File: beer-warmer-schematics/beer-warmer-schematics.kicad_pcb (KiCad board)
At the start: 4 copper layers, 60 x 42.8 mm, 41 parts, among them J1 USB_C_Receptacle_USB2.0_14P, J2 Screw_Terminal_01x02, J3 Conn_01x07_Socket, J4 Conn_01x07_Socket, J5 Conn_01x04_Pin, J6 Screw_Terminal_01x03, Q1 AOD4184A, U2 LM2596S-5, U3 CH224K, U4 INA219AxDCN

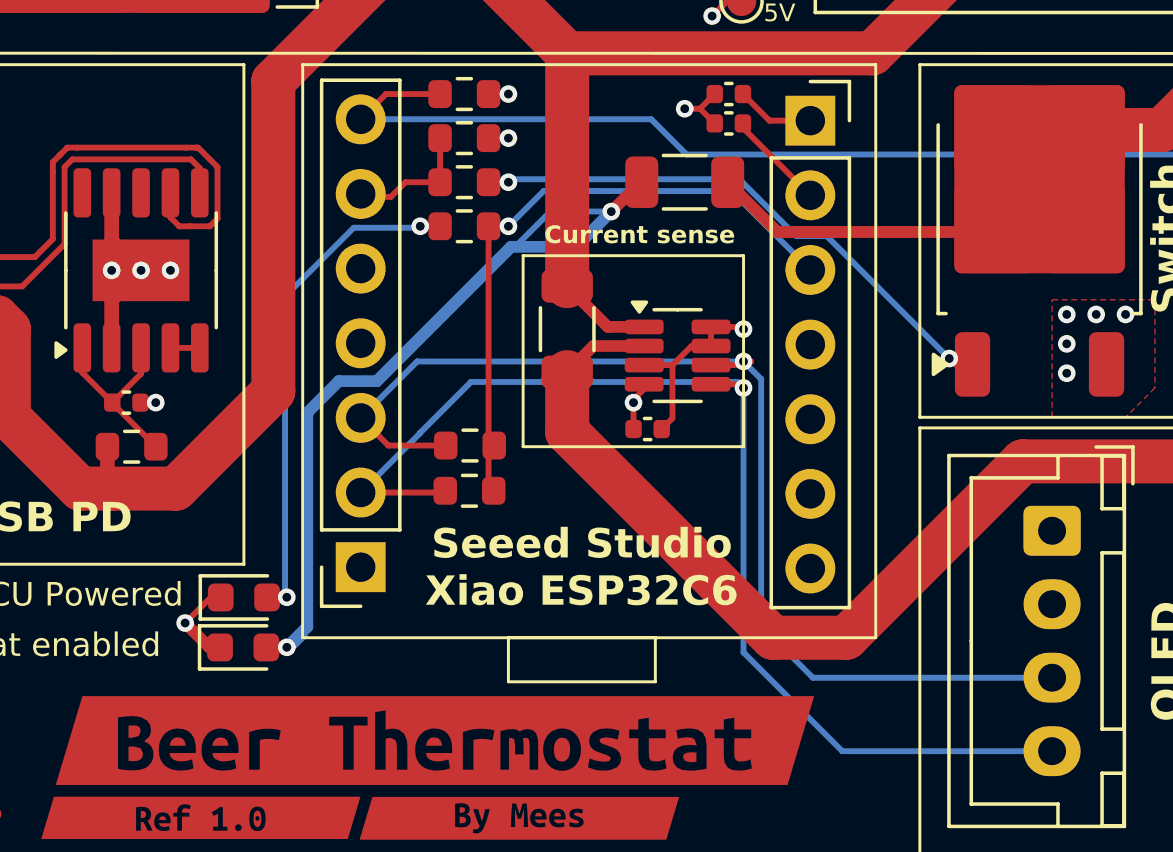
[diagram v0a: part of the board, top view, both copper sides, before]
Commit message: fix active led, bottom silkscreen
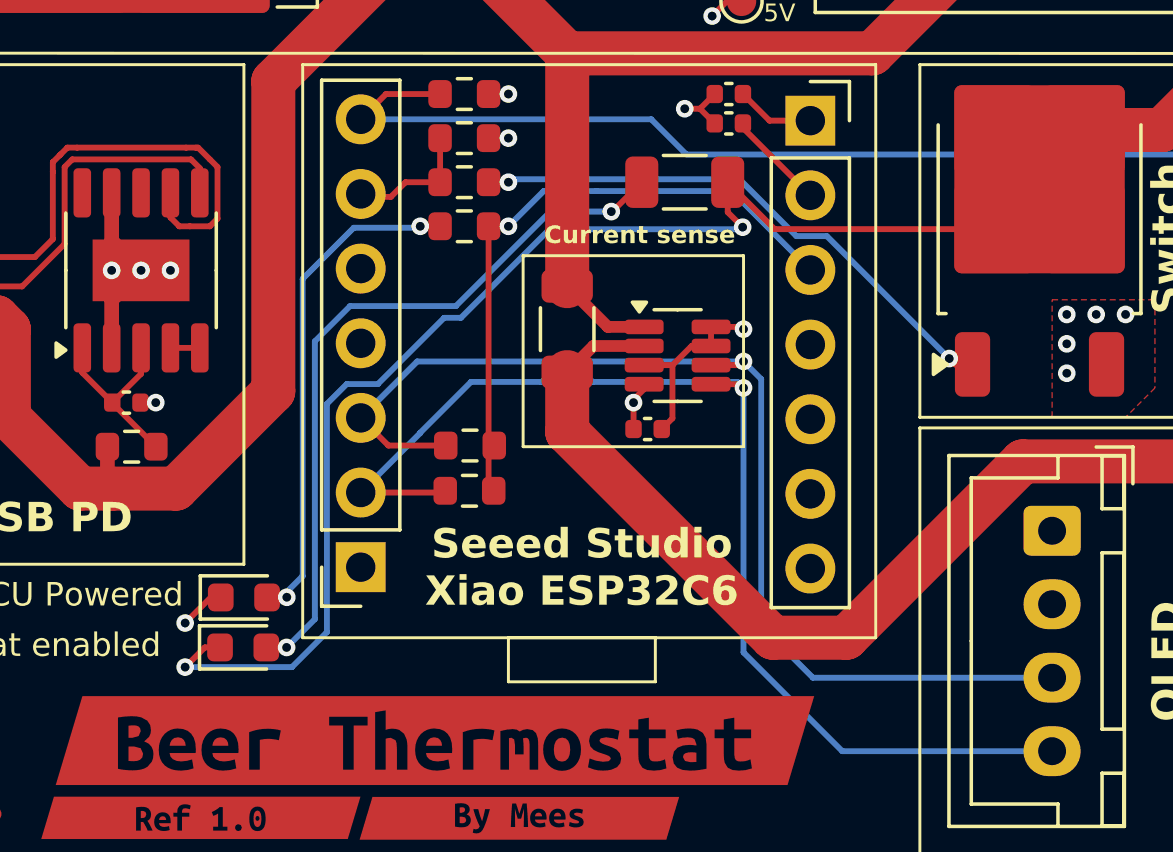
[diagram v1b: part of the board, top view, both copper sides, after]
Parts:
- J1: value USB_C_Receptacle_USB2.0_14P -> USB_C_Receptacle_6P
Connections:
- D2 pad 1: GND -> HEAT-
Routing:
- net HEAT-: track 32.5 -> 55.8 mm, vias 0 -> 2
- net Net-(D2-A): track 45.4 -> 24.5 mm
- net GND: track 42.8 -> 41.3 mm
- net SDA: track 38.7 -> 38.1 mm
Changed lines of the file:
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@@
 			(layers "F.Cu" "F.Mask" "F.Paste")
 			(roundrect_rratio 0.25)
-			(net 22 "GND")
+			(net 24 "HEAT-")
 			(pinfunction "K")
 			(pintype "passive")
@@
 			)
 		)
-		(property "Value" "USB_C_Receptacle_USB2.0_14P"
+		(property "Value" "USB_C_Receptacle_6P"
 			(at 0 4.725 270)
 			(unlocked yes)
@@
 		(layer "F.SilkS")
 	)
+	(gr_rect
+		(start 169.5 79.5)
+		(end 179 89.5)
+		(stroke
+			(width 0.1)
+			(type default)
+		)
+		(fill no)
+		(layer "B.SilkS")
+	)
+	(gr_rect
+		(start 169.5 91)
+		(end 179 106)
+		(stroke
+			(width 0.1)
+			(type default)
+		)
+		(fill no)
+		(layer "B.SilkS")
+	)
 	(gr_line
 		(start 182 110)
@@
 		)
 	)
+	(gr_text "-\n\n\n+"
+		(at 172.5 87.5 0)
+		(layer "B.SilkS")
+		(effects
+			(font
+				(size 1 1)
+				(thickness 0.2)
+				(bold yes)
+			)
+			(justify left bottom mirror)
+		)
+	)
 	(gr_text "Heater\nout"
-		(at 171.5 86.58 0)
+		(at 169 82.5 0)
 		(layer "B.SilkS")
 		(effects
@@
 		)
 	)
-	(gr_text "SIG\n5V\nGND"
-		(at 171.5 101.58 0)
+	(gr_text "SIG\n\n\n5V\n\n\nGND"
+		(at 173 104 0)
 		(layer "B.SilkS")
 		(effects
 			(font
-				(size 1.5 1.5)
-				(thickness 0.3)
+				(size 1 1)
+				(thickness 0.2)
 				(bold yes)
 			)
@@
 	)
 	(gr_text "Temp\nprobe"
-		(at 171.5 94.08 0)
+		(at 168.778727 93.941909 0)
 		(layer "B.SilkS")
 		(effects
@@
 	)
 	(segment
-		(start 149.5375 91)
-		(end 149.5 91)
-		(width 0.4)
+		(start 148.5 92)
+		(end 148.5375 92)
+		(width 0.2)
 		(layer "F.Cu")
 		(net 4)
 	)
 	(segment
-		(start 137.456833 106.829694)
-		(end 137.460788 106.825739)
-		(width 0.4)
+		(start 136.762359 106.830388)
+		(end 136.761665 106.829694)
+		(width 0.2)
 		(layer "F.Cu")
 		(net 4)
 	)
 	(segment
-		(start 149.5 91)
-		(end 148.5 92)
+		(start 149.5375 91)
+		(end 149.5 91)
 		(width 0.4)
 		(layer "F.Cu")
@@
 	)
 	(segment
-		(start 136.761665 106.829694)
-		(end 137.456833 106.829694)
-		(width 0.4)
+		(start 148.5375 92)
+		(end 149.5375 91)
+		(width 0.2)
 		(layer "F.Cu")
 		(net 4)
@@
 	)
 	(via
-		(at 137.460788 106.825739)
+		(at 137.452508 106.830388)
 		(size 0.6)
 		(drill 0.3)
@@
 	)
 	(segment
-		(start 148.5 92)
-		(end 147.299 93.201)
-		(width 0.4)
-		(layer "B.Cu")
-		(net 4)
-	)
-	(segment
-		(start 138.160531 98.839469)
-		(end 138.160531 106.125996)
-		(width 0.4)
-		(layer "B.Cu")
-		(net 4)
-	)
-	(segment
-		(start 138.160531 106.125996)
-		(end 137.460788 106.825739)
-		(width 0.4)
-		(layer "B.Cu")
-		(net 4)
-	)
-	(segment
-		(start 138.060531 98.939469)
-		(end 138.060531 106.221217)
-		(width 0.2)
-		(layer "B.Cu")
-		(net 4)
-	)
-	(segment
-		(start 146.4279 92)
-		(end 140.5589 97.869)
+		(start 138.41362 105.869276)
+		(end 137.452508 106.830388)
 		(width 0.2)
 		(layer "B.Cu")
@@
 	)
 	(segment
-		(start 139.231 97.769)
-		(end 138.160531 98.839469)
-		(width 0.4)
-		(layer "B.Cu")
-		(net 4)
-	)
-	(segment
-		(start 147.299 93.201)
-		(end 145.08548 93.201)
-		(width 0.4)
-		(layer "B.Cu")
-		(net 4)
-	)
-	(segment
 		(start 148.5 92)
 		(end 146.4279 92)
@@
 	)
 	(segment
-		(start 138.060531 106.221217)
-		(end 138.060531 106.439469)
+		(start 138.41362 96.41362)
+		(end 138.41362 105.869276)
 		(width 0.2)
 		(layer "B.Cu")
@@
 	)
 	(segment
-		(start 145.08548 93.201)
-		(end 140.51748 97.769)
-		(width 0.4)
-		(layer "B.Cu")
-		(net 4)
-	)
-	(segment
-		(start 138.060531 106.439469)
-		(end 137.5 107)
+		(start 139.61329 95.21395)
+		(end 138.41362 96.41362)
 		(width 0.2)
 		(layer "B.Cu")
@@
 	)
 	(segment
-		(start 140.5589 97.869)
-		(end 139.131 97.869)
+		(start 143.21395 95.21395)
+		(end 139.61329 95.21395)
 		(width 0.2)
 		(layer "B.Cu")
@@
 	)
 	(segment
-		(start 140.51748 97.769)
-		(end 139.231 97.769)
-		(width 0.4)
-		(layer "B.Cu")
-		(net 4)
-	)
-	(segment
-		(start 139.131 97.869)
-		(end 138.060531 98.939469)
+		(start 146.4279 92)
+		(end 143.21395 95.21395)
 		(width 0.2)
 		(layer "B.Cu")
@@
 	)
 	(segment
-		(start 153.25747 97.099)
-		(end 153.132467 97.224003)
+		(start 151.89497 97.224003)
+		(end 152.874997 97.224003)
 		(width 0.2)
 		(layer "F.Cu")
@@
 	)
 	(segment
-		(start 153.132467 97.224003)
-		(end 151.89497 97.224003)
+		(start 152.874997 97.224003)
+		(end 153 97.099)
 		(width 0.2)
 		(layer "F.Cu")
@@
 	)
 	(segment
-		(start 153.25747 97.099)
-		(end 141.896 97.099)
+		(start 155.360525 107.860525)
+		(end 153.601 106.101)
 		(width 0.2)
 		(layer "B.Cu")
@@
 	)
 	(segment
-		(start 155.360525 107.860525)
-		(end 153.601 106.101)
+		(start 141.896 97.099)
+		(end 139.975 99.02)
 		(width 0.2)
 		(layer "B.Cu")
@@
 	)
 	(segment
-		(start 141.896 97.099)
-		(end 139.975 99.02)
+		(start 153 97.099)
+		(end 141.896 97.099)
 		(width 0.2)
 		(layer "B.Cu")
@@
 	)
 	(segment
-		(start 142 92.5)
-		(end 141.949 92.551)
+		(start 141.949 92.551)
+		(end 139.73624 92.551)
 		(width 0.2)
 		(layer "B.Cu")
@@
 	)
 	(segment
-		(start 141.949 92.551)
-		(end 139.73624 92.551)
+		(start 138 94.28724)
+		(end 138 104.4)
+		(width 0.2)
+		(layer "B.Cu")
+		(net 20)
+	)
+	(segment
+		(start 138 104.4)
+		(end 137.4 105)
 		(width 0.2)
 		(layer "B.Cu")
@@
 	(segment
 		(start 139.73624 92.551)
-		(end 137.4 94.88724)
+		(end 138 94.28724)
 		(width 0.2)
 		(layer "B.Cu")
@@
 	)
 	(segment
-		(start 137.4 94.88724)
-		(end 137.4 105)
+		(start 142 92.5)
+		(end 141.949 92.551)
 		(width 0.2)
 		(layer "B.Cu")
@@
 	)
 	(segment
-		(start 135.186665 106.829694)
-		(end 134.829694 106.829694)
-		(width 0.4)
-		(layer "F.Cu")
-		(net 22)
-	)
-	(segment
 		(start 131.5 91.3625)
 		(end 131.5 91.5)
@@
 	)
 	(segment
-		(start 134.829694 106.829694)
-		(end 134 106)
-		(width 0.4)
-		(layer "F.Cu")
-		(net 22)
-	)
-	(segment
 		(start 151.89497 95.924003)
 		(end 152.924003 95.924003)
@@
 	)
 	(segment
+		(start 134.670306 106.829694)
+		(end 134 107.5)
+		(width 0.2)
+		(layer "F.Cu")
+		(net 24)
+	)
+	(segment
 		(start 161.5475 92.575)
 		(end 161.426162 92.696338)
@@
 	)
 	(segment
-		(start 161.426162 92.696338)
-		(end 154.158838 92.696338)
-		(width 0.4)
+		(start 152.4625 91)
+		(end 152.4625 92.022128)
+		(width 0.2)
+		(layer "F.Cu")
+		(net 24)
+	)
+	(segment
+		(start 152.4625 92.022128)
+		(end 152.970186 92.529814)
+		(width 0.2)
 		(layer "F.Cu")
 		(net 24)
@@
 	)
 	(segment
-		(start 154.158838 92.696338)
-		(end 152.4625 91)
-		(width 0.4)
+		(start 135.186665 106.829694)
+		(end 134.670306 106.829694)
+		(width 0.2)
 		(layer "F.Cu")
 		(net 24)
 	)
+	(via
+		(at 152.970186 92.529814)
+		(size 0.6)
+		(drill 0.3)
+		(layers "F.Cu" "B.Cu")
+		(net 24)
+	)
+	(via
+		(at 134 107.5)
+		(size 0.6)
+		(drill 0.3)
+		(layers "F.Cu" "B.Cu")
+		(net 24)
+	)
+	(segment
+		(start 138.824 98.54324)
+		(end 138.824 106.308839)
+		(width 0.2)
+		(layer "B.Cu")
+		(net 24)
+	)
+	(segment
+		(start 152.970186 92.529814)
+		(end 152.899 92.601)
+		(width 0.2)
+		(layer "B.Cu")
+		(net 24)
+	)
+	(segment
+		(start 138.824 106.308839)
+		(end 137.632839 107.5)
+		(width 0.2)
+		(layer "B.Cu")
+		(net 24)
+	)
+	(segment
+		(start 152.899 92.601)
+		(end 146.399 92.601)
+		(width 0.2)
+		(layer "B.Cu")
+		(net 24)
+	)
+	(segment
+		(start 146.399 92.601)
+		(end 143.38505 95.61495)
+		(width 0.2)
+		(layer "B.Cu")
+		(net 24)
+	)
+	(segment
+		(start 137.632839 107.5)
+		(end 134 107.5)
+		(width 0.2)
+		(layer "B.Cu")
+		(net 24)
+	)
+	(segment
+		(start 139.49824 97.869)
+		(end 138.824 98.54324)
+		(width 0.2)
+		(layer "B.Cu")
+		(net 24)
+	)
+	(segment
+		(start 140.5589 97.869)
+		(end 139.49824 97.869)
+		(width 0.2)
+		(layer "B.Cu")
+		(net 24)
+	)
+	(segment
+		(start 142.81295 95.61495)
+		(end 140.5589 97.869)
+		(width 0.2)
+		(layer "B.Cu")
+		(net 24)
+	)
+	(segment
+		(start 143.38505 95.61495)
+		(end 142.81295 95.61495)
+		(width 0.2)
+		(layer "B.Cu")
+		(net 24)
+	)

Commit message: incorporated some feedback
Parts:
- removed C4: 1uF, Capacitor_SMD:C_0402_1005Metric
- moved R8 1.54 mm to (143.7, 101.5)
- moved R9 1.54 mm to (143.7, 100.0)
- moved C1 1.00 mm to (152.5, 89.0)
- turned R2 to 0 degrees
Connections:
- J3 pad 2: Net-(J3-Pin_2) -> GND
- R2 pad 1: GND -> D1
- R2 pad 2: D1 -> GND
- R8 pad 1: SDA -> SCL
- R9 pad 1: SCL -> SDA
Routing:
- net Net-(J3-Pin_2): track 3.40 -> 0.00 mm
- net GND: track 41.3 -> 39.9 mm

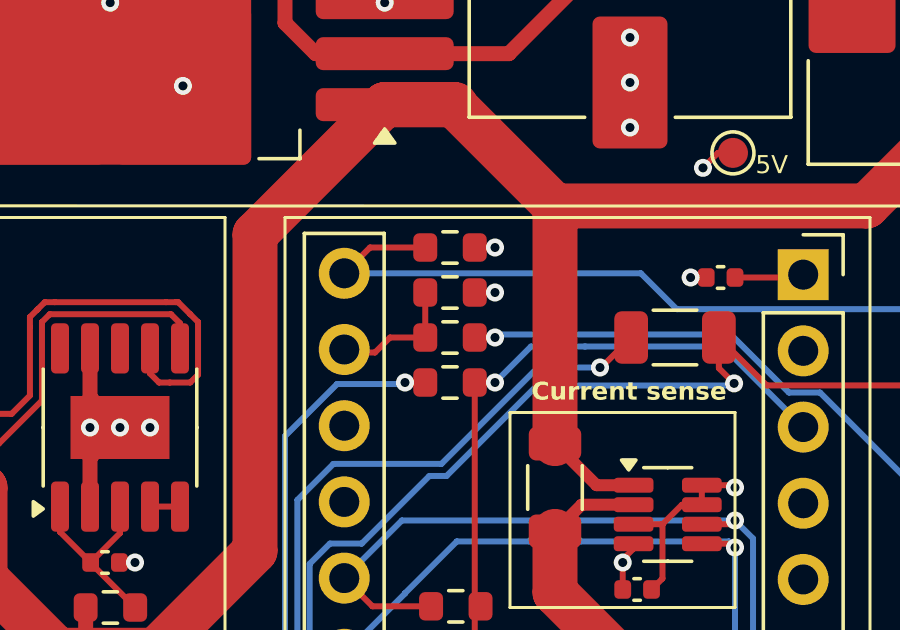
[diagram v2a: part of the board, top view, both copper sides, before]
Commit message: low side driver
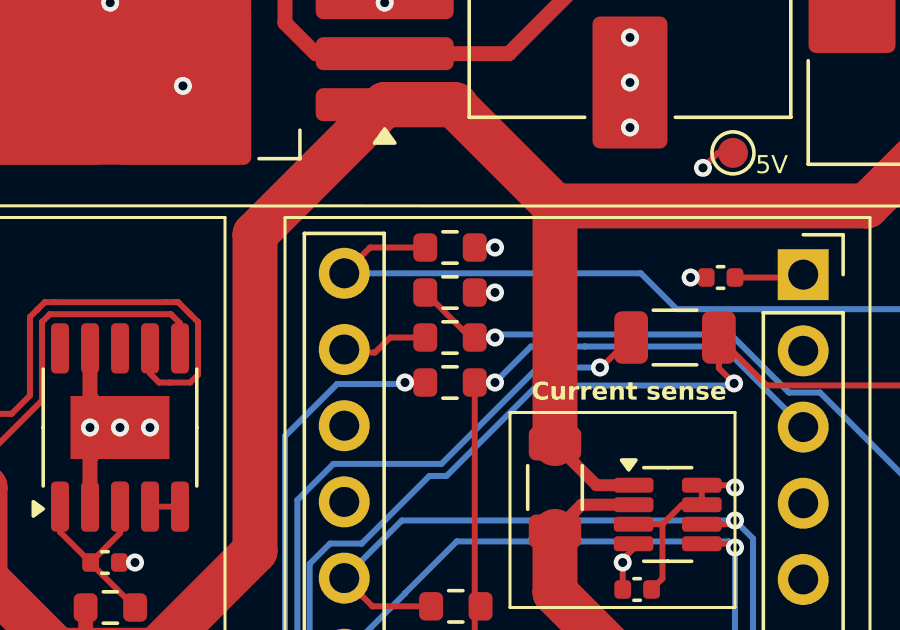
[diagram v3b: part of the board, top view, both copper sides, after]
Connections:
- R2 pad 1: D1 -> Net-(Q1-G)
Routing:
- net Net-(Q1-G): track 19.2 -> 21.5 mm
- net D1: track 5.01 -> 3.51 mm
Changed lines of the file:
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@@
 			(layers "F.Cu" "F.Mask" "F.Paste")
 			(roundrect_rratio 0.25)
-			(net 17 "D1")
+			(net 24 "Net-(Q1-G)")
 			(pintype "passive")
 		)
@@
 	)
 	(segment
-		(start 142.675 89.5)
-		(end 142.675 91)
-		(width 0.2)
-		(layer "F.Cu")
-		(net 17)
-	)
-	(segment
 		(start 140.835 88)
 		(end 142.675 88)
@@
 	)
 	(segment
+		(start 144.175 91)
+		(end 142.675 89.5)
+		(width 0.2)
+		(layer "F.Cu")
+		(net 24)
+	)
+	(segment
 		(start 144.325 91)
 		(end 144.902 91)
 		(width 0.2)
 		(layer "F.Cu")
+		(net 24)
+	)
+	(segment
+		(start 144.325 91)
+		(end 144.175 91)
+		(width 0.2)
+		(layer "F.Cu")

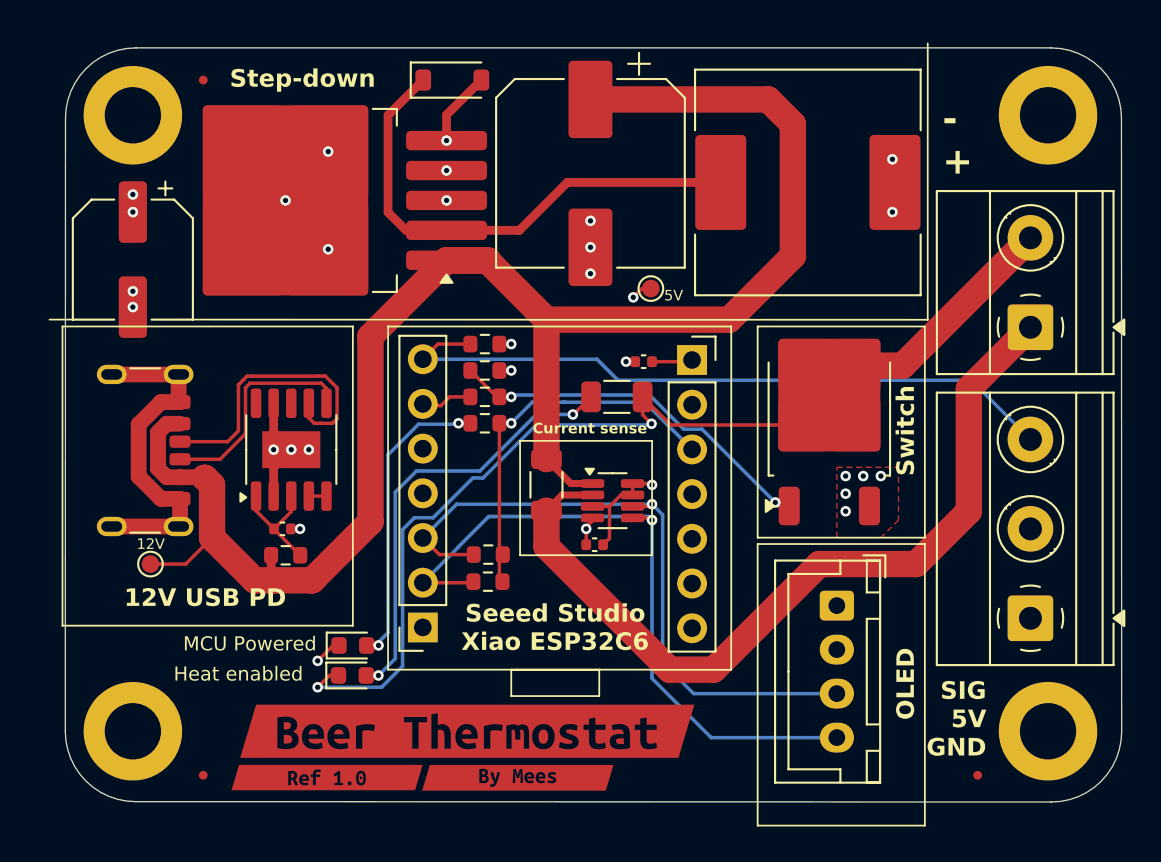
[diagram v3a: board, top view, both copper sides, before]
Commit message: different step down
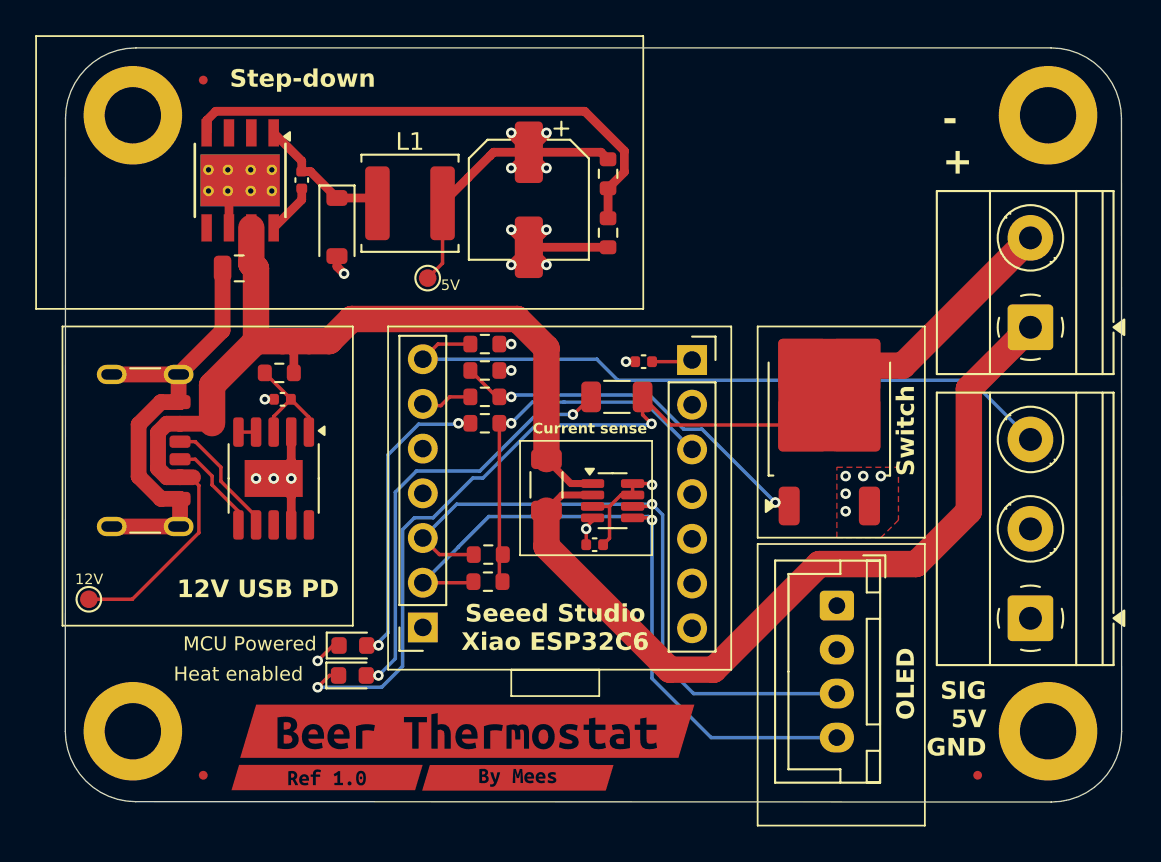
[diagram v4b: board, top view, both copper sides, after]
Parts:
- added C7: 10nF, Capacitor_SMD:C_0402_1005Metric, F.Cu at (133.1, 78.7)
- added R11: 3.3K, Resistor_SMD:R_0603_1608Metric, F.Cu at (150.5, 81.7)
- added R5: 10K, Resistor_SMD:R_0603_1608Metric, F.Cu at (150.5, 78.3)
- C2: value 680uF -> 10uF; footprint Capacitor_SMD:CP_Elec_10x10.5 -> Capacitor_SMD:C_0805_2012Metric
- L1: value 33uH -> 15uH; footprint Inductor_SMD:L_SXN_SMDRI127 -> Inductor_SMD:L_Changjiang_FNR5040S
- U2: value LM2596S-5 -> TPS5430DDA; footprint Package_TO_SOT_SMD:TO-263-5_TabPin3 -> Package_SO:TI_SO-PowerPAD-8_ThermalVias
- moved C3 22.8 mm to (146.0, 79.8)
- moved L1 22.6 mm to (139.2, 80.0)
- moved C2 20.7 mm to (129.5, 83.7), turned to 180 degrees
- moved TP2 12.7 mm to (140.3, 84.3)
- moved D1 10.6 mm to (135.1, 81.3), turned to -90 degrees
- moved R1 10.4 mm to (131.8, 89.6), turned to 180 degrees
- moved C6 7.36 mm to (132.0, 91.1), turned to 0 degrees
- moved U2 4.23 mm to (129.6, 78.7), turned to -90 degrees
- moved TP1 4.03 mm to (121.0, 102.5)
- moved U3 1.92 mm to (131.5, 95.6), turned to -90 degrees
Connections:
- U2 pad 1: VBUS -> Net-(D1-K)
- U2 pad 2: Net-(D1-K) -> unconnected-(U2-NC-Pad2)
- U2 pad 3: GND -> unconnected-(U2-NC-Pad3)
- U2 pad 4: +5V -> Net-(U2-VSENSE)
- U2 pad 5: GND -> unconnected-(U2-EN-Pad5)
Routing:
- net VBUS: track 99.8 -> 61.4 mm
- net Net-(U2-VSENSE): track 0.00 -> 29.8 mm
- net Net-(D1-K): track 28.8 -> 7.91 mm
- net +5V: track 5.87 -> 25.8 mm, vias 8 -> 6
- net GND: track 39.9 -> 56.9 mm, vias 23 -> 18
- net Net-(J1-CC1): track 16.7 -> 7.03 mm
- net Net-(J1-CC2): track 12.6 -> 5.61 mm
- net Net-(U2-PH): track 0.00 -> 2.90 mm

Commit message: routing overhaul
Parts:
- added J7: Conn_01x07_Socket, Library:PinHeader_1x07_P2.54mm_Vertical, F.Cu at (154.3, 76.7)
- added J8: Conn_01x07_Socket, Library:PinHeader_1x07_P2.54mm_Vertical, F.Cu at (169.6, 73.0)
- moved C5 21.1 mm to (165.1, 85.0)
- moved R10 21.1 mm to (162.4, 81.6)
- moved U4 21.1 mm to (166.1, 82.5)
- moved R3 9.50 mm to (151.0, 100.5)
- moved C1 1.13 mm to (153.0, 90.0), turned to -90 degrees
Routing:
- net D0: track 39.5 -> 98.7 mm
- net Net-(J4-Pin_1): track 0.00 -> 53.6 mm
- net SCL: track 39.7 -> 87.9 mm, vias 1 -> 2
- net SDA: track 38.1 -> 84.3 mm
- net Net-(J3-Pin_7): track 0.00 -> 37.8 mm
- net Net-(J4-Pin_4): track 0.00 -> 37.3 mm
- net Net-(J3-Pin_6): track 0.00 -> 33.1 mm
- net Net-(J4-Pin_5): track 0.00 -> 32.6 mm
- net HEAT+: track 47.6 -> 17.7 mm
- net D1: track 3.51 -> 32.1 mm
- net Net-(J3-Pin_5): track 0.00 -> 28.3 mm
- net Net-(J3-Pin_4): track 0.00 -> 23.6 mm
- net +3V3: track 21.9 -> 40.7 mm, vias 1 -> 0
- net VBUS: track 61.4 -> 71.9 mm
- net GND: track 56.9 -> 65.9 mm, vias 18 -> 16
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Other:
- board text added: "43mm"
- board text added: "60mm"
- board text added: "D0 D1 D2 D3 D4 D5 D6 5V GND 3V3 D10 D9 D8 D7"
